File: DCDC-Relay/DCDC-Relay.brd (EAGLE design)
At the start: 45.7 x 50.8 mm, 9 parts, among them J1 1X2-3.5MM, J2 1X2-3.5MM, K2 CMX60D5, U5 TSR 1-2450

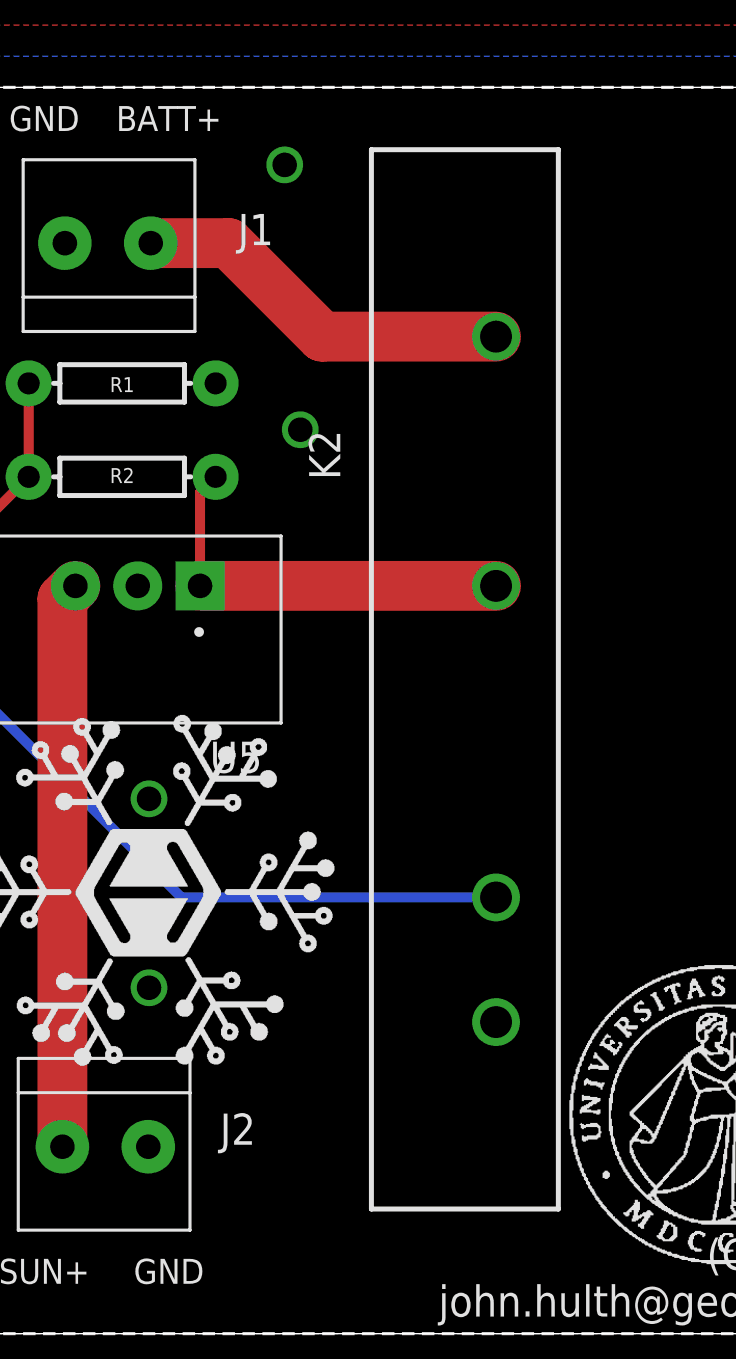
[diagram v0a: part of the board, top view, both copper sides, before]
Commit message: Wheatstone ordered
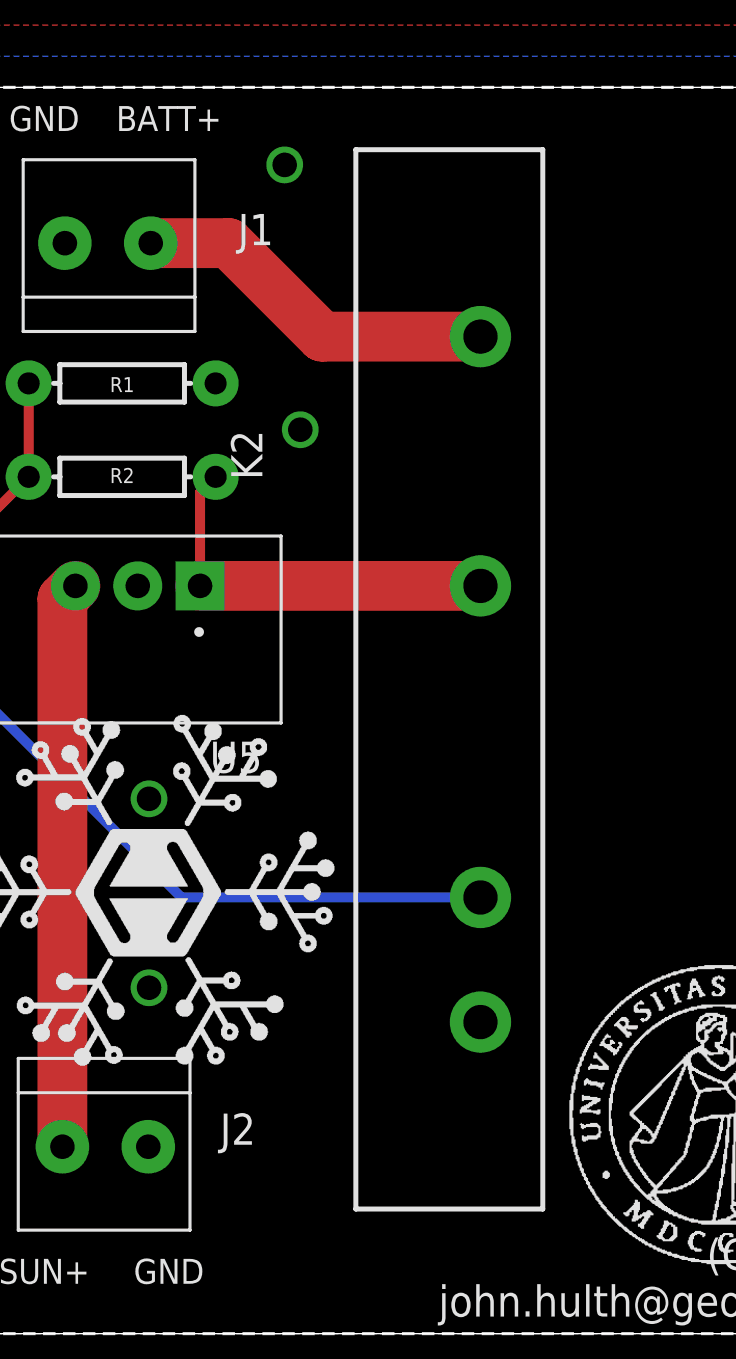
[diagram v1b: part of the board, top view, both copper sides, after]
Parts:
- U5: value TSR 1-2450 -> TSR 1-2465
- moved K2 3.17 mm to (31.8, 5.08)
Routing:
- net BATT+: track 15.7 -> 15.0 mm
- net A5: track 29.0 -> 28.3 mm
- net 24V: track 16.8 -> 16.1 mm
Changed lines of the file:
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@@
 <elements>
 <element name="U$1" library="UIO-John" package="WASPMOTE_V1.5" value="WASPMOTE_V1.5" x="0" y="0" smashed="yes"/>
-<element name="U5" library="DC-DC Converter" package="173010535" package3d_urn="urn:adsk.eagle:package:20779907/3" value="TSR 1-2450" x="15.24" y="30.48" smashed="yes" rot="R180">
+<element name="U5" library="DC-DC Converter" package="173010535" package3d_urn="urn:adsk.eagle:package:20779907/3" value="TSR 1-2465" x="15.24" y="30.48" smashed="yes" rot="R180">
 <attribute name="CREATED_BY" value="PCBLayout.com" x="54.61" y="11.43" size="1.778" layer="27" rot="R180" display="off"/>
 <attribute name="DIGIKEY_PARTNO" value="732-173010535-ND" x="54.61" y="11.43" size="1.778" layer="27" rot="R180" display="off"/>
@@
 <attribute name="MPN" value="173010535" x="54.61" y="11.43" size="1.778" layer="27" rot="R180" display="off"/>
 <attribute name="NAME" x="20.32" y="24.13" size="1.27" layer="25" rot="R180"/>
-<attribute name="VALUE" x="21.59" y="33.02" size="1.27" layer="27" rot="R270"/>
+<attribute name="VALUE" x="10.16" y="26.035" size="1.27" layer="27"/>
 </element>
 <element name="J2" library="adafruit" library_urn="urn:adsk.eagle:library:420" package="1X2-3.5MM" package3d_urn="urn:adsk.eagle:package:6240635/1" value="1X2-3.5MM" x="13.97" y="7.62" smashed="yes" rot="R180">
@@
 <attribute name="VALUE" x="14.605" y="33.909" size="0.6096" layer="27" font="vector" ratio="20" align="top-center"/>
 </element>
-<element name="K2" library="DCDC-Relay" package="CMX60D5" value="CMX60D5" x="34.925" y="5.08" smashed="yes" rot="R90">
-<attribute name="NAME" x="22.225" y="36.83" size="1.27" layer="25" rot="R270"/>
-<attribute name="VALUE" x="22.225" y="25.4" size="1.27" layer="27" rot="R270"/>
+<element name="K2" library="DCDC-Relay" package="CMX60D5" value="CMX60D5" x="31.75" y="5.08" smashed="yes" rot="R90">
+<attribute name="NAME" x="19.05" y="36.83" size="1.27" layer="25" rot="R270"/>
+<attribute name="VALUE" x="26.035" y="27.94" size="1.27" layer="27" rot="R270"/>
 </element>
 </elements>
@@
 <wire x1="6.86" y1="27.94" x2="17.02" y2="17.78" width="0.4064" layer="16"/>
 <contactref element="K2" pad="3"/>
-<wire x1="17.02" y1="17.78" x2="29.845" y2="17.78" width="0.4064" layer="16"/>
+<wire x1="17.02" y1="17.78" x2="29.21" y2="17.78" width="0.4064" layer="16"/>
 </signal>
 <signal name="A6">
@@
 <wire x1="17.78" y1="34.29" x2="17.78" y2="30.48" width="0.4064" layer="1"/>
 <contactref element="K2" pad="2"/>
-<wire x1="17.78" y1="30.48" x2="29.845" y2="30.48" width="2.032" layer="1"/>
+<wire x1="17.78" y1="30.48" x2="29.21" y2="30.48" width="2.032" layer="1"/>
 </signal>
 <signal name="BATT+">
@@
 <wire x1="18.945" y1="44.45" x2="15.77" y2="44.45" width="2.032" layer="1"/>
 <contactref element="K2" pad="1"/>
-<wire x1="22.755" y1="40.64" x2="29.845" y2="40.64" width="2.032" layer="1"/>
+<wire x1="22.755" y1="40.64" x2="29.21" y2="40.64" width="2.032" layer="1"/>
 </signal>
 </signals>
